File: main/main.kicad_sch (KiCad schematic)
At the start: 12 parts, among them SW1 TVAF06-A020B-R, U1 STM32F411CEUx

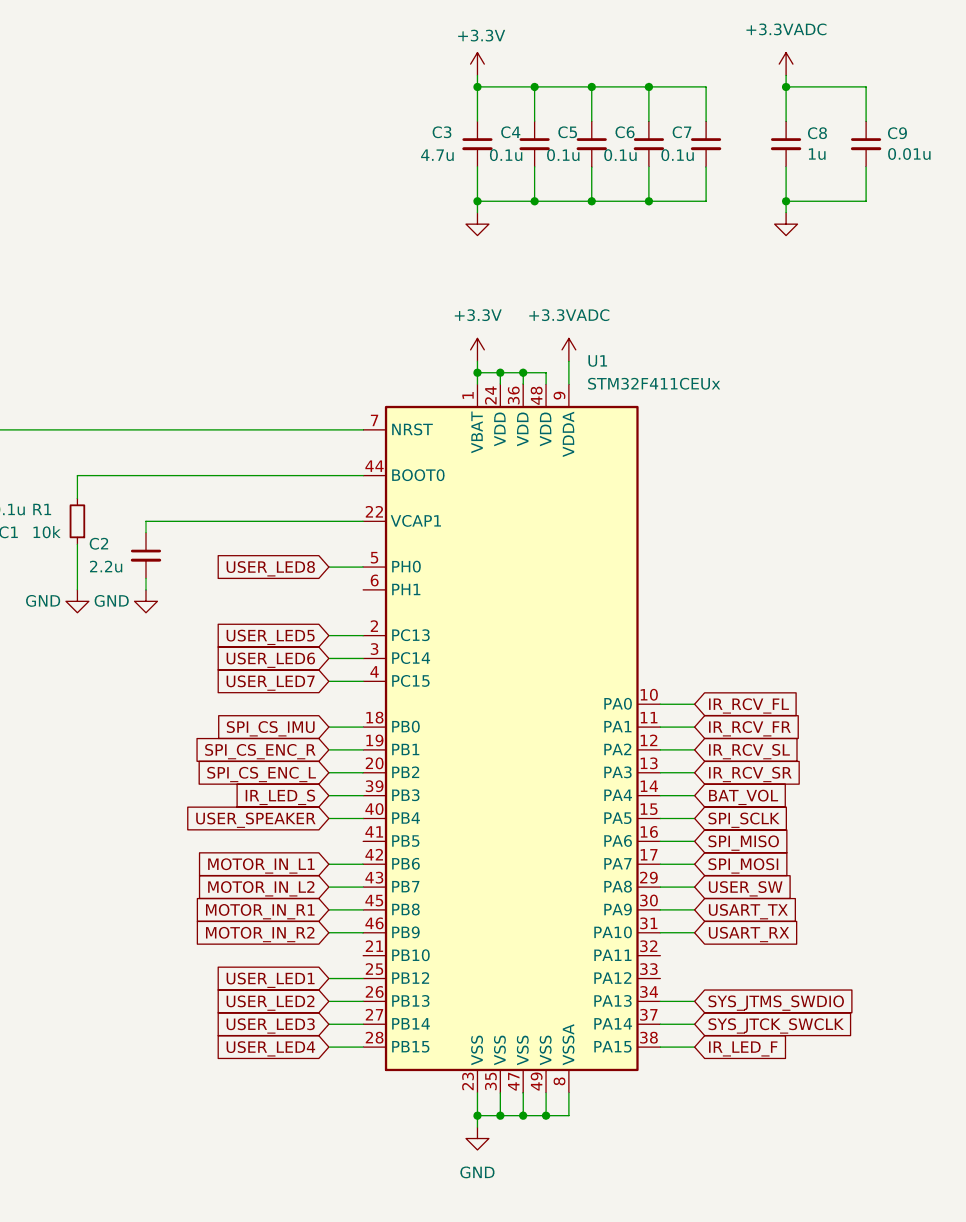
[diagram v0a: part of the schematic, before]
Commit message: feat: update main board
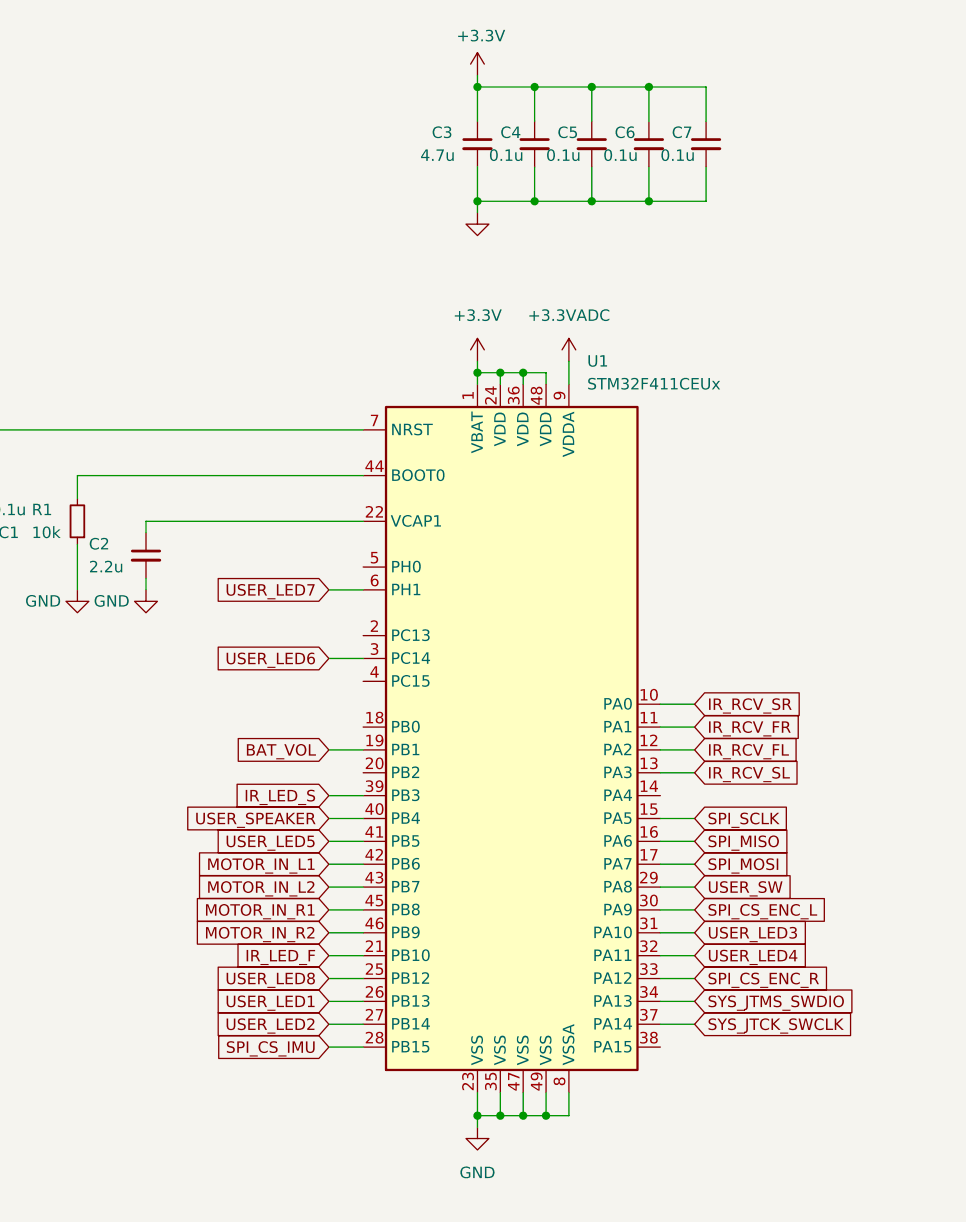
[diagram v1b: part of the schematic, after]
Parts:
- removed C8: 1u, Capacitor_SMD:C_0402_1005Metric, symbol Device:C_Small
- removed C9: 0.01u, Capacitor_SMD:C_0201_0603Metric, symbol Device:C_Small
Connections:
- net USART_RX is gone; now on net USER_LED3: U1.31 (PA10)
- net USART_TX is gone; now on net SPI_CS_ENC_L: U1.30 (PA9)
- net BAT_VOL: now also U1.19 (PB1); no longer U1.14 (PA4)
- net IR_LED_F: now also U1.21 (PB10); no longer U1.38 (PA15)
- net IR_RCV_FL: now also U1.12 (PA2); no longer U1.10 (PA0)
- net IR_RCV_SL: now also U1.13 (PA3); no longer U1.12 (PA2)
- net IR_RCV_SR: now also U1.10 (PA0); no longer U1.13 (PA3)
- net SPI_CS_ENC_L: no longer U1.20 (PB2)
- net SPI_CS_ENC_R: now also U1.33 (PA12); no longer U1.19 (PB1)
- net SPI_CS_IMU: now also U1.28 (PB15); no longer U1.18 (PB0)
- net USER_LED1: now also U1.26 (PB13); no longer U1.25 (PB12)
- net USER_LED2: now also U1.27 (PB14); no longer U1.26 (PB13)
- net USER_LED3: no longer U1.27 (PB14)
- net USER_LED4: now also U1.32 (PA11); no longer U1.28 (PB15)
- net USER_LED5: now also U1.41 (PB5); no longer U1.2 (PC13)
- net USER_LED7: now also U1.6 (PH1); no longer U1.4 (PC15)
- net USER_LED8: now also U1.25 (PB12); no longer U1.5 (PH0)
